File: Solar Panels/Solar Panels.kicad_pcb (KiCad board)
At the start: 2 copper layers, 113 x 82.5 mm, 58 parts, among them J2 5040500891

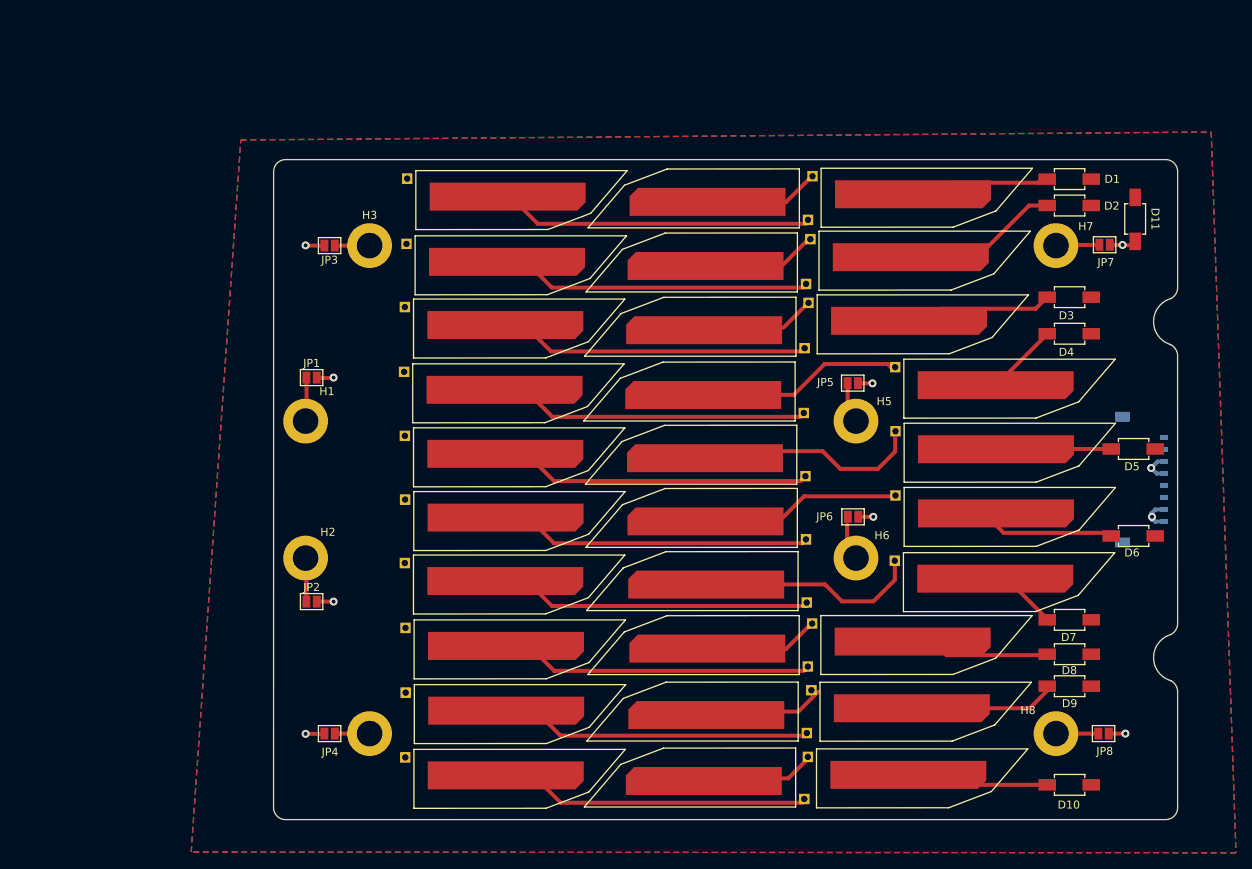
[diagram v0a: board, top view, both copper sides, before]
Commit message: August 20th Changes
Finished setting up the PCB board (haven't started the PCB board yet)
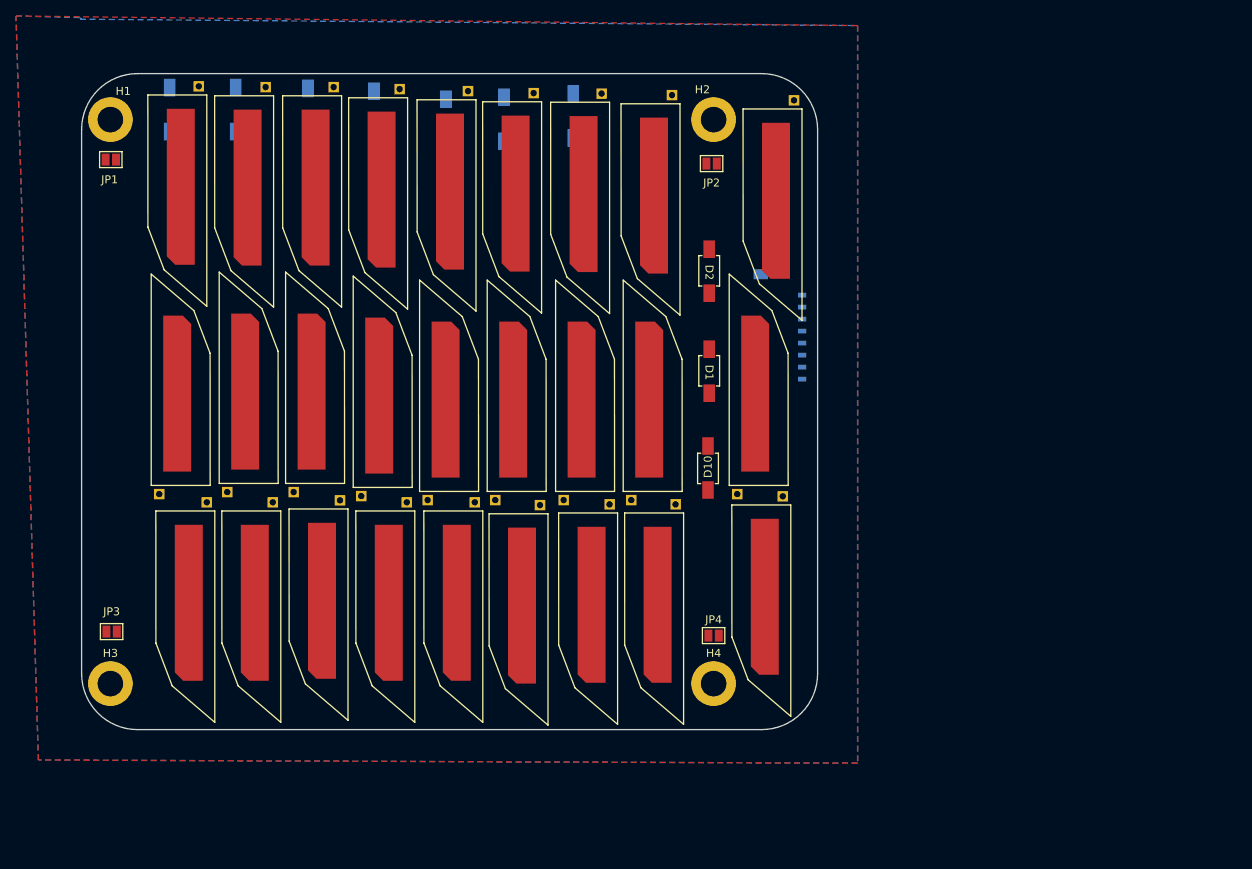
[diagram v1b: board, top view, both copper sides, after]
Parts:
- removed D11: PMEG10020AELPX, Solar Panel Library:PMEG10020AELPX
- removed H5, H6, H7, H8: MountingHole_Pad, MountingHole:MountingHole_3.2mm_M3_DIN965_Pad
- removed J2: 5040500891, Solar Panel Library:5040500891
- removed JP5, JP6, JP7, JP8: Jumper_2_Open, Jumper:SolderJumper-2_P1.3mm_Open_Pad1.0x1.5mm
- removed SC28, SC29, SC30: Solar_Cell, Solar Panel Library:TrisolX Solar Wings
- added J1: 5040500891, Solar Panels Library:CON_5040500891, B.Cu at (141.1, 102.2)
- D1, D10, D2: value PMEG10020AELPX -> D; footprint Solar Panel Library:PMEG10020AELPX -> Solar Panels Library:PMEG10020AELPX
- D3, D4, D5, D6, D7, D8, D9: value PMEG10020AELPX -> D; footprint Solar Panel Library:PMEG10020AELPX -> Solar Panels Library:PMEG10020AELPX; moved to B.Cu
- SC1, SC10, SC11, SC12, SC13, SC14, SC15, SC16, SC17, SC18, SC19, SC2, SC20, SC21, SC22, SC23, SC24, SC25, SC26, SC27, SC3, SC4, SC5, SC6, SC7, SC8, SC9: footprint Solar Panel Library:TrisolX Solar Wings -> Solar Panels Library:Trisolx Wings
- moved D9 133.4 mm to (62.2, 68.5), turned to -90 degrees
- moved D8 124.3 mm to (70.5, 68.5), turned to -90 degrees
- moved D7 114.3 mm to (79.5, 68.7), turned to -90 degrees
- moved SC25 111.5 mm to (63.4, 75.4), turned to 180 degrees
- moved D6 108.5 mm to (87.8, 69.0), turned to -90 degrees
- moved SC22 99.8 mm to (71.7, 75.5), turned to 180 degrees
- moved SC19 96.8 mm to (80.2, 75.5), turned to 180 degrees
- moved D5 95.0 mm to (96.8, 70.0), turned to -90 degrees
- moved SC16 85.5 mm to (88.5, 75.8), turned to 180 degrees
- moved SC26 78.7 mm to (63.0, 106.8), turned to 0 degrees
- moved D4 75.4 mm to (104.0, 69.8), turned to -90 degrees
- moved H2 74.9 mm to (130.0, 69.8)
- moved JP2 74.1 mm to (129.8, 75.2), turned to 180 degrees
- moved SC13 74.0 mm to (97.0, 76.0), turned to 180 degrees
- moved SC23 67.6 mm to (71.5, 106.5), turned to 0 degrees
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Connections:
- D10 pad 2: Net-(SC28-+) -> GND
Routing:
- net Net-(SC23--): track 39.2 -> 0.00 mm
- net Net-(SC14--): track 39.2 -> 0.00 mm
- net Net-(SC11--): track 39.0 -> 0.00 mm
- net Net-(SC2--): track 38.9 -> 0.00 mm
- net Net-(SC17--): track 36.8 -> 0.00 mm
- net Net-(SC20--): track 36.7 -> 0.00 mm
- net Net-(SC8--): track 36.3 -> 0.00 mm
- net Net-(SC5--): track 36.2 -> 0.00 mm
- net Net-(SC29--): track 35.1 -> 0.00 mm
- net Net-(SC26--): track 34.7 -> 0.00 mm
- net Net-(SC19--): track 25.9 -> 0.00 mm
- net Net-(SC13--): track 25.3 -> 0.00 mm
- net Net-(D9-A): track 19.3 -> 0.00 mm
- net Net-(D2-A): track 19.0 -> 0.00 mm
- net Net-(D8-A): track 18.7 -> 0.00 mm
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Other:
- board size 113 x 82.5 mm -> 92 x 82 mm

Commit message: Finished initial draft of the 1U
Finished routing initial 1U draft to be reviewed by Parker and structural.
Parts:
- moved SC2 0.79 mm to (135.5, 106.0)
- moved SC3 0.79 mm to (136.6, 125.9)
- moved D3 0.25 mm to (112.5, 69.2), turned to -90 degrees
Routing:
- net Net-(D1-A): track 0.00 -> 51.8 mm
- net +VDC: track 0.00 -> 43.7 mm, vias 0 -> 6
- net Net-(SC4--): track 0.00 -> 43.4 mm
- net Net-(SC1--): track 0.00 -> 41.6 mm
- net Net-(SC25--): track 0.00 -> 40.9 mm
- net Net-(SC13--): track 0.00 -> 40.7 mm
- net Net-(SC19--): track 0.00 -> 40.4 mm
- net Net-(SC16--): track 0.00 -> 40.4 mm
- net Net-(SC7--): track 0.00 -> 40.3 mm
- net Net-(SC22--): track 0.00 -> 40.2 mm
- net Net-(SC10--): track 0.00 -> 40.0 mm
- net Net-(D2-A): track 0.00 -> 15.8 mm
- net Net-(SC26--): track 0.00 -> 15.3 mm
- net Net-(SC23--): track 0.00 -> 15.3 mm
- net Net-(SC20--): track 0.00 -> 15.1 mm
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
